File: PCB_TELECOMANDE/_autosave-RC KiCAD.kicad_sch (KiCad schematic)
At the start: 49 parts, among them J1 USB4085, Q2 BD140, U1 TL431AIDBZR, U12 LM317T, U2 D3V3XA4B10LP, U3 ESP32-S3-WROOM-2-N32R8V, U4 TLV75801PDBV, U6 LM317T

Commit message: New BMS
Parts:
- removed BT1: 1043P, 1043P:BAT_1043P, symbol 1043P:1043P
- removed BT2: 1043P, Footprints:BAT_1043P, symbol 1043P:1043P
- removed C1, C2: JMK325ABJ107MM-P, Footprints:CAPC3225X280N, symbol JMK325ABJ107MM-P:JMK325ABJ107MM-P
- removed D1, D2, D3, D4: DSS14UTR, DSS14UTR:SODFL3618X110N, symbol DSS14UTR:DSS14UTR
- removed LED1: APT1608SGC, Footprints:LED_APT1608SGC_KNB, symbol APT1608SGC:APT1608SGC
- removed Q2: BD140, Footprints:TO229P760X270X1364-3, symbol BD140:BD140
- removed R1, R10, R2: RMCF1206FT20R0, RMCF1206FT20R0:RESC3216X70N, symbol RMCF1206FT20R0:RMCF1206FT20R0
- removed R13: CRM2512-FX-2R00ELF, Footprints:RESC6331X80N, symbol CRM2512-FX-2R00ELF:CRM2512-FX-2R00ELF
- removed R15: RMCF2512JT3K30, RMCF2512JT3K30:RESC6332X70N, symbol RMCF2512JT3K30:RMCF2512JT3K30
- removed R16: CRCW12101K40FKEA, CRCW12101K40FKEA:RESC3225X60N, symbol CRCW12101K40FKEA:CRCW12101K40FKEA
- removed R3: RMCF1206FT1K00, RMCF1206FT1K00:RESC3216X70N, symbol RMCF1206FT1K00:RMCF1206FT1K00
- removed R4: RMCF2512JT330R, RMCF2512JT330R:RESC6332X70N, symbol RMCF2512JT330R:RMCF2512JT330R
- removed S1: 400BWMSP1R2BLKSM6QE, Footprints:SW_400BWMSP1R2BLKSM6QE, symbol 400BWMSP1R2BLKSM6QE:400BWMSP1R2BLKSM6QE
- removed U1: TL431AIDBZR, TL431AIDBZR:SOT95P237X112-3N, symbol TL431AIDBZR:TL431AIDBZR
- removed U12, U6: LM317T, Footprints:TO254P1054X470X1955-3, symbol LM317T:LM317T
- removed U2: D3V3XA4B10LP, Package_DFN_QFN:Diodes_UDFN-10_1.0x2.5mm_P0.5mm, symbol Power_Protection:D3V3XA4B10LP
- added C1, C10, C9: 0.1uF, symbol Device:C_Small
- added C2: 0.33uF, symbol Device:C_Small
- added CR1: SMF9.0CA, SOD-123F_LTF, symbol SMF9_0CA:SMF9.0CA
- added F1: Polyfuse_Small, symbol Device:Polyfuse_Small
- added F2: Fuse_Small, symbol Device:Fuse_Small
- added J4: BAT2_CON, 1990009:PHOENIX_1990009, symbol 1990009:1990009
- added J5: BAT1_CON, 1990009:PHOENIX_1990009, symbol 1990009:1990009
- added L1: 60R @ 100MHz, symbol Device:L_Small
- added Q1: PMV45EN2, Package_TO_SOT_SMD:SOT-23-3, symbol Simulation_SPICE:NMOS
- added R1, R2: 5.1K, symbol Device:R_Small
- added R10: 160, symbol Device:R_Small
- added R12: 0, TestPoint:TestPoint_2Pads_Pitch2.54mm_Drill0.8mm, symbol Device:R_Small
- added R3: 1k, symbol Device:R_Small
- added R4: 100, symbol Device:R_Small
- added TP1: GND, Connector_Pin:Pin_D1.0mm_L10.0mm, symbol Connector:TestPoint
- added TP2: VBUS, Connector_Pin:Pin_D1.0mm_L10.0mm, symbol Connector:TestPoint
- added TP3, TP5, TP7: TestPoint, symbol Connector:TestPoint
- added TP4: BAT1+, symbol Connector:TestPoint
- added TP6: BAT2+, symbol Connector:TestPoint
- added TP8: PACK-, symbol Connector:TestPoint
- added TP9: PACK+, symbol Connector:TestPoint
- added U1: BQ29200DRBT, BQ29200DRBT:IC_DRV8601DRBT, symbol BQ29200DRBT:BQ29200DRBT
- added U2: BQ24133RGYR, BQ24133RGYR:QFN50P550X350X100-25N, symbol BQ24133RGYR:BQ24133RGYR
- C3, C4, C5, C6, C7, C8: footprint (none) -> Capacitor_SMD:C_0805_2012Metric
- J3: footprint Footprints:CONN_S2B-PH-QUE-S_JST -> Connector_JST:JST_PH_B2B-PH-QUE_1x02_P2.00mm_Vertical
- R11, R8, R9: footprint (none) -> Resistor_SMD:R_1206_3216Metric
- R5: value 5.1k -> 260
- R6: value 5.1k -> 100
- R7: footprint (none) -> Resistor_SMD:R_0805_2012Metric
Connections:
- net D+ is gone; now on net USB_D+: J1.A6 (DP1), J1.B6 (DP2)
- net D- is gone; now on net USB_D-: J1.A7 (DN1), J1.B7 (DN2)
- net GND: now also C2.1, L1.1, U1.5 (GND), U1.9 (EPAD); no longer J1.A1 (GND), J1.A12 (GND__1), J1.B1 (GND__2), J1.B12 (GND__3), J1.S1 (SHELL), J1.S2 (SHELL__1), J1.S3 (SHELL__2), J1.S4 (SHELL__3), R5.2, R6.2
- net at J1.A5 (CC1): now also R1.1; no longer R6.1
- net at J1.A4 (VBUS), J1.A9 (VBUS__1), J1.B4 (VBUS__2)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: now also TP2.1
- net at R5.1: now also R6.1, J4.1, J5.2, TP4.1, TP7.1; no longer J1.B5 (CC2)
- new net: F2.1, J4.2, R10.1, R12.1, R4.2, TP6.1
- new net: CR1.1, F1.2, TP3.1
- new net: Q1.1 (D), R12.2
- new net: Q1.2 (G), R3.2
- new net: J1.B5 (CC2), R2.1
- new net: C1.1, R4.1, U1.7 (VDD)
- new net: R3.1, U1.8 (OUT)
- new net: C9.1, R10.2
- new net: C10.1, C9.2, R5.2
- new net GNDREF: CR1.2, J1.A1 (GND), J1.A12 (GND__1), J1.B1 (GND__2), J1.B12 (GND__3), J1.S1 (SHELL), J1.S2 (SHELL__1), J1.S3 (SHELL__2), J1.S4 (SHELL__3), L1.2, R1.2, R2.2, TP1.1
- new net PACK+: F2.2, TP9.1
- new net PACK-: C1.2, C10.2, J5.1, Q1.3 (S), TP5.1, TP8.1
- no-connect marks 36 -> 30
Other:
- note added: "BATTERY PROTECTION SYSTEM"
- note added: "USB"
- note removed: "5V -> 4.2V"
- note removed: "600mA limit"
- note removed: "BMS PCB"
- note removed: "CARP Alexandru"
- moved on the sheet: BOOT_SW1, C3, C4, C5, C6, C7, C8, D5, D6, H1, H2, H3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

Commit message: Improving Charging efficency to 90%
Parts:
- removed TP1: GND, Connector_Pin:Pin_D1.0mm_L10.0mm, symbol Connector:TestPoint
- added C11, C12: 0.1uF, symbol Device:C_Small
- added C13: 4.7uF, symbol Device:C_Small
- added C14: 100nF, symbol Device:C_Small
- added D1: ESDA25W, ESDA25W:SOT65P210X110-3N, symbol ESDA25W:ESDA25W
- added D2: BAT60A, Diode_SMD:D_SOD-323, symbol Diode:BAT60A
- added R13, R14, R15: 100K, symbol Device:R_Small
- added RESET_SW2: PTS810_SJM_250_SMTR_LFS, Footprints:SW_PTS810_SJM_250_SMTR_LFS, symbol PTS810_SJM_250_SMTR_LFS:PTS810_SJM_250_SMTR_LFS
- added U5: STUSB4500QTR, STUSB4500QTR:QFN50P400X400X90-25N, symbol STUSB4500QTR:STUSB4500QTR
- added U6: CYPD3177-24LQ, Package_DFN_QFN:QFN-24-1EP_4x4mm_P0.5mm_EP2.75x2.75mm, symbol Interface_USB:CYPD3177-24LQ
- R1, R2: value 5.1K -> R_Small
- TP3: footprint (none) -> TestPoint:TestPoint_Pad_D1.5mm
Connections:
- net GND: now also C11.2, C12.2, C13.2, C14.2, D1.3, R13.2, R14.1, R15.1, U5.10 (GND), U5.25 (EP)
- net GNDREF: no longer R1.2, R2.2
- net at R1.1: now also R2.1; no longer J1.A5 (CC1)
- net at J1.B5 (CC2): no longer R2.1
- new net: R1.2, R13.1
- new net: C13.1, C14.1, U6.18 (VBUS_IN)
- new net: D1.2, U5.1 (CC1DB), U5.2 (CC1)
- new net: C11.1, U5.21 (VREG_1V2)
- new net: C12.1, D2.2 (A), U5.23 (VREG_2V7)
- new net: D1.1, U5.4 (CC2), U5.5 (CC2DB)
- new net: R15.2, RESET_SW2.3, RESET_SW2.4, U5.6 (RESET)
- new net: RESET_SW2.1, RESET_SW2.2
- new net: R14.2, R2.2
- new net: U6.19 (GND), U6.22 (GND), U6.25 (GND)
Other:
- moved on the sheet: C7, C8, D5, D6, H1, H2, H3, H4, R11, R8, R9, U2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

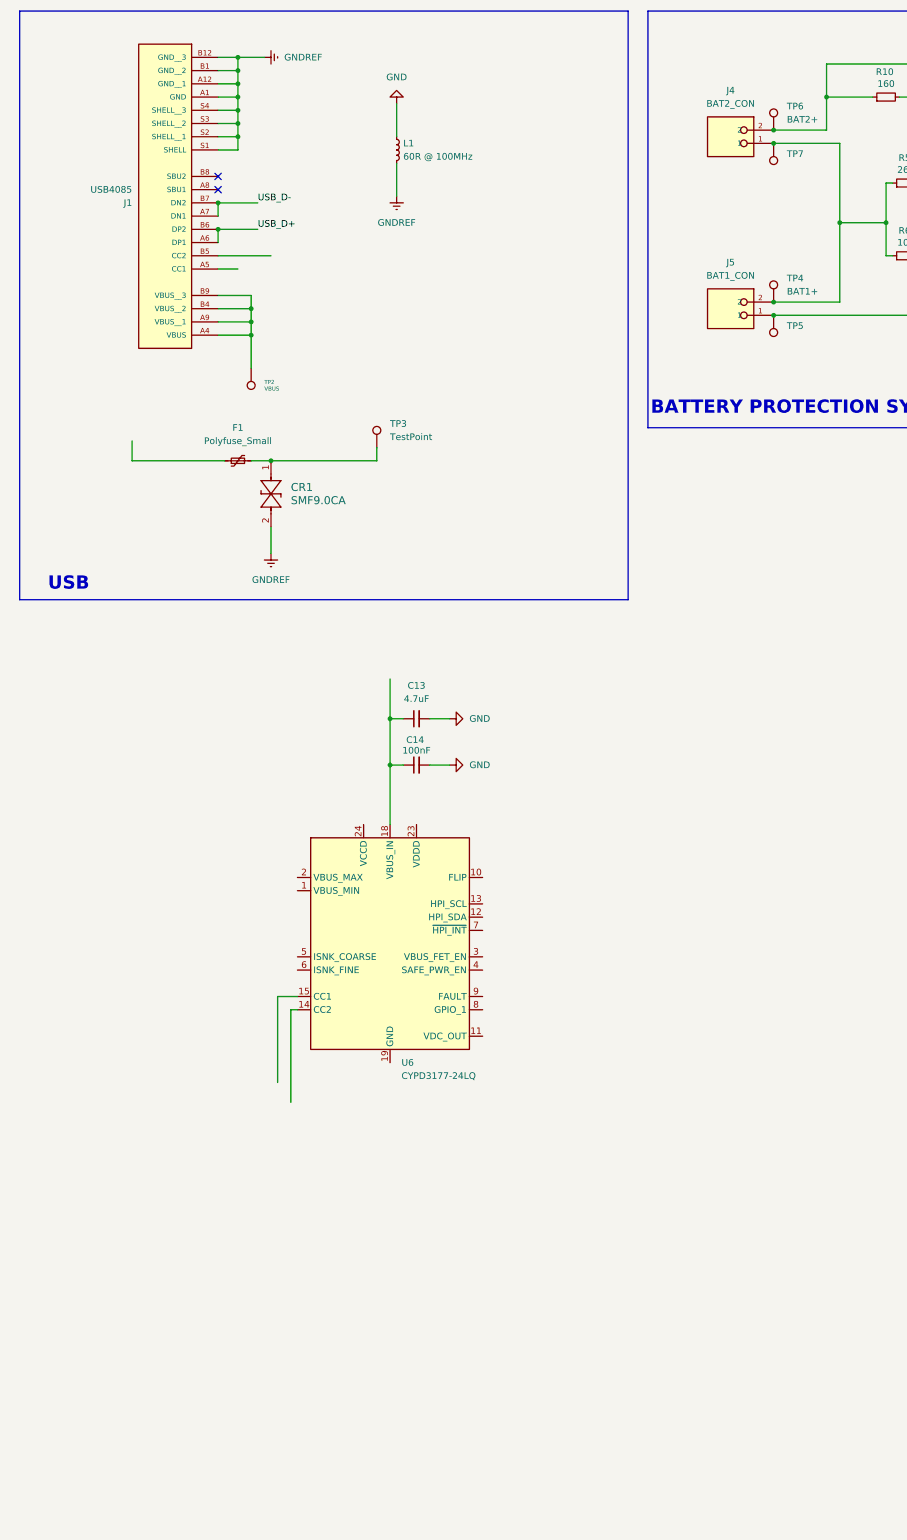
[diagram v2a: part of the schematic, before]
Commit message: Filesys Reorg + PD Negociator schematics
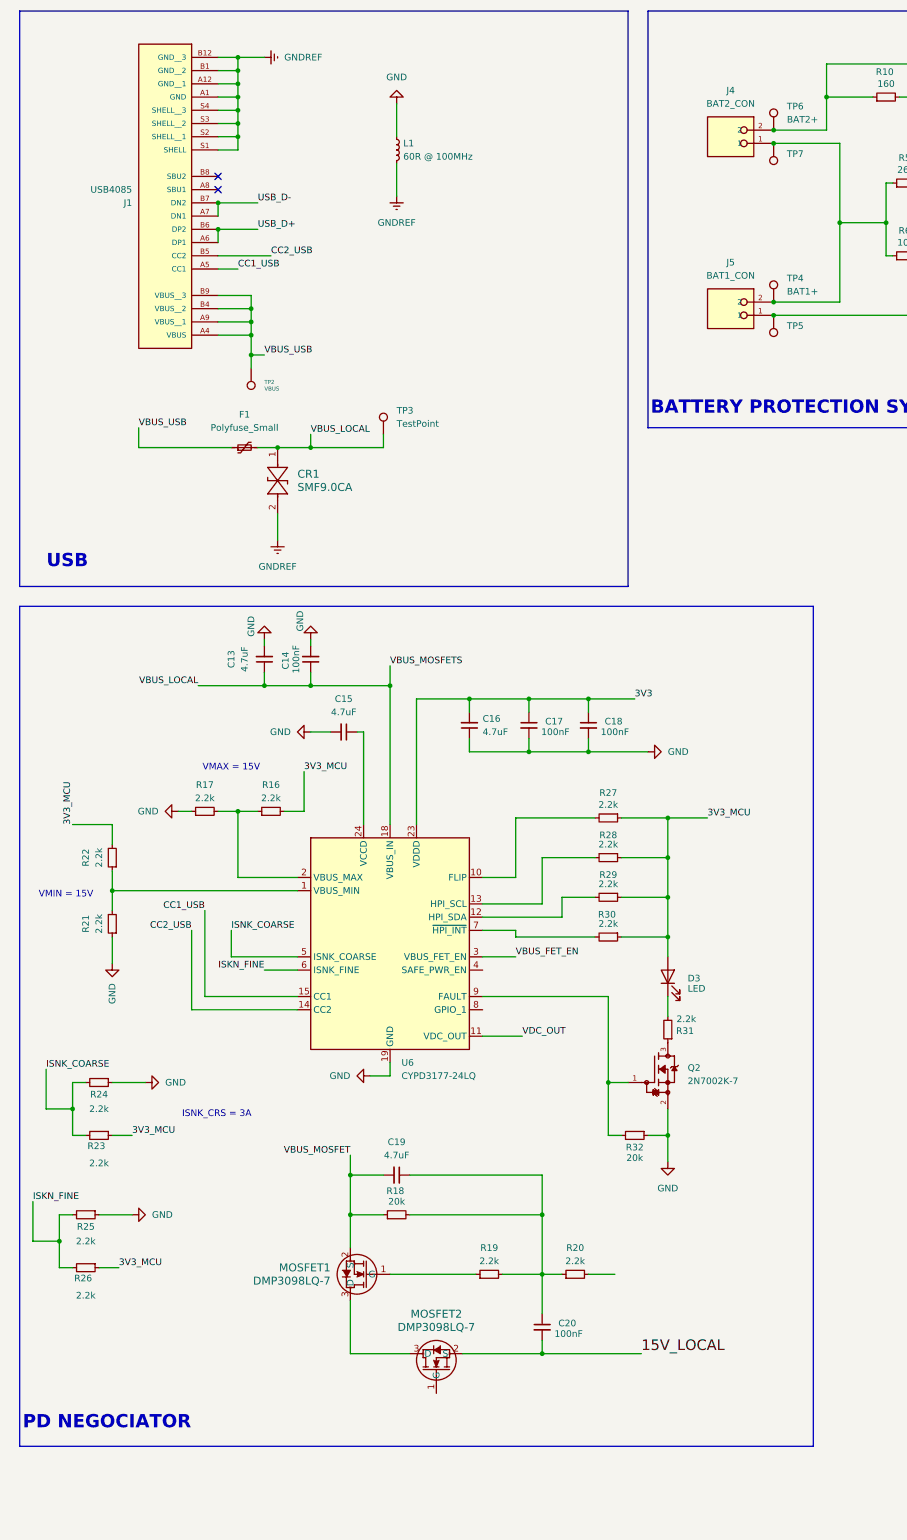
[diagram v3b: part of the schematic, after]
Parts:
- added C15, C16, C19: 4.7uF, symbol Device:C_Small
- added C17, C18, C20: 100nF, symbol Device:C_Small
- added D3: LED, LED_SMD:LED_0603_1608Metric, symbol Device:LED
- added MOSFET1, MOSFET2: DMP3098LQ-7, SOT-23_DMP3098LQ_DIO, symbol DMP3098LQ_7:DMP3098LQ-7
- added Q2: 2N7002K-7, 2N7002K-7:SOT91P240X110-3N, symbol 2N7002K-7:2N7002K-7
- added R16, R17, R19, R20, R21, R22, R23, R24, R25, R26, R27, R28, R29, R30, R31: 2.2k, symbol Device:R_Small
- added R18, R32: 20k, symbol Device:R_Small
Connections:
- net 3V3: now also U6.23 (VDDD), C16.2, C17.1, C18.1
- net GND: now also U6.19 (GND), U6.22 (GND), U6.25 (GND), C15.2, C16.1, C17.2, C18.2, Q2.2, R17.1, R21.1, R24.1, R25.1, R32.1
- net VBUS_LOCAL: now reaches C13.1, C14.1, U6.18 (VBUS_IN)
- net VBUS_LOCAL: now also CR1.1, F1.2, TP3.1
- net at U6.1 (VBUS_MIN): now also R21.2, R22.1
- net at U6.10 (FLIP): now also R27.2
- net VDC_OUT: now reaches U6.11 (VDC_OUT)
- net at U6.12 (HPI_SDA): now also R29.2
- net at U6.13 (HPI_SCL): now also R28.2
- net CC2_USB: now reaches U6.14 (CC2)
- net CC2_USB: now also J1.B5 (CC2)
- net CC1_USB: now reaches U6.15 (CC1)
- net CC1_USB: now also J1.A5 (CC1)
- net at U6.2 (VBUS_MAX): now also R16.1, R17.2
- net at U6.24 (VCCD): now also C15.1
- net VBUS_FET_EN: now reaches U6.3 (VBUS_FET_EN)
- net ISNK_COARSE: now reaches U6.5 (ISNK_COARSE)
- net ISNK_COARSE: now also R23.2, R24.2
- net ISKN_FINE: now reaches U6.6 (ISNK_FINE)
- net ISKN_FINE: now also R25.2, R26.2
- net at U6.7 (~{HPI_INT}): now also R30.2
- net at U6.9 (FAULT): now also Q2.1, R32.2
- net VBUS_USB: now reaches J1.A4 (VBUS), J1.A9 (VBUS__1), J1.B4 (VBUS__2), J1.B9 (VBUS__3), TP2.1
- net VBUS_USB: now also F1.1
- new net: C19.1, C20.1, R18.2, R19.2, R20.1
- new net: MOSFET1.1 (G), R19.1
- new net: D3.1 (K), R31.2
- new net: MOSFET1.3 (D), MOSFET2.3 (D)
- new net: Q2.3, R31.1
- new net 15V_LOCAL: C20.2, MOSFET2.2 (S)
- new net 3V3_MCU: D3.2 (A), R16.2, R22.2, R23.1, R26.1, R27.1, R28.1, R29.1, R30.1
- new net VBUS_MOSFET: C19.2, MOSFET1.2 (S), R18.1
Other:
- note added: "ISNK_CRS = 3A"
- note added: "PD NEGOCIATOR"
- note added: "VMAX = 15V"
- note added: "VMIN = 15V"
- moved on the sheet: C13, C14, CR1, F1, TP3
